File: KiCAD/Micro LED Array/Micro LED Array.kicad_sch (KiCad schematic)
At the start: 15 parts, among them J1 Conn_02x07_1mm

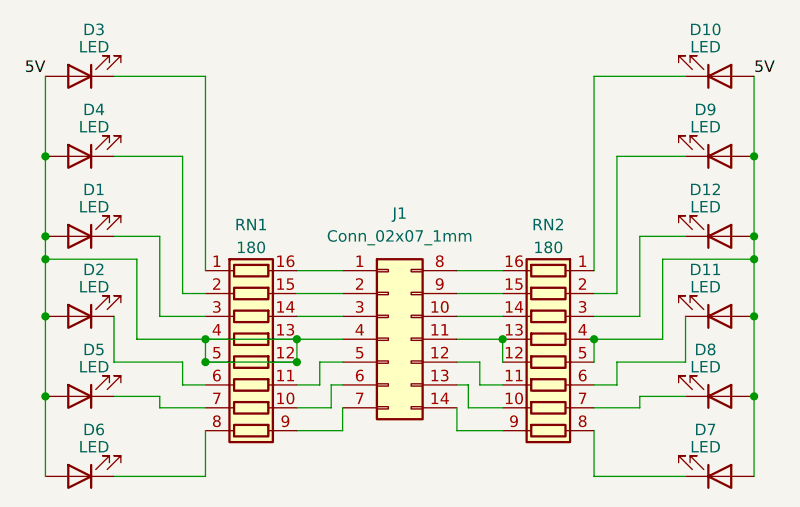
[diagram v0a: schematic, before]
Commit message: Add holes for electrodes
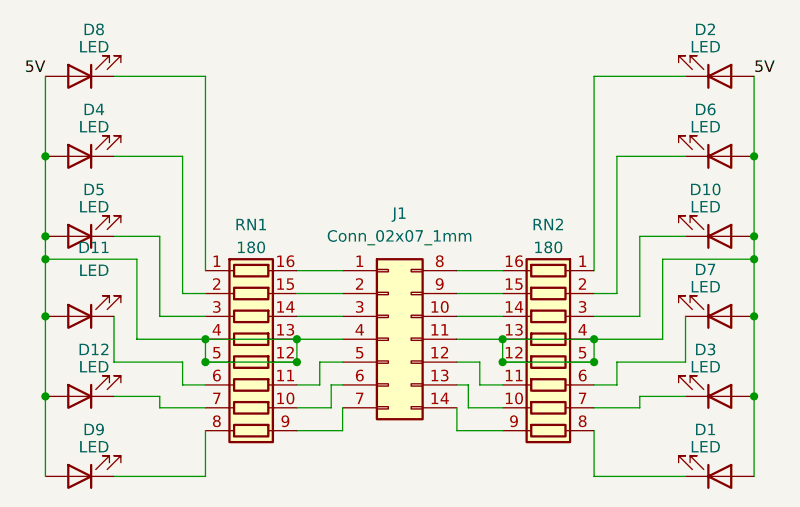
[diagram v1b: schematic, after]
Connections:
- net 5V: now also J1.11 (Pin_11), RN2.12 (R5.2), RN2.13 (R4.2)
- net at RN1.1 (R1.1): now also D8.1 (K); no longer D3.1 (K)
- net at RN1.3 (R3.1): now also D5.1 (K); no longer D1.1 (K)
- net at RN1.6 (R6.1): now also D11.1 (K); no longer D2.1 (K)
- net at RN1.7 (R7.1): now also D12.1 (K); no longer D5.1 (K)
- net at RN1.8 (R8.1): now also D9.1 (K); no longer D6.1 (K)
- net at RN2.2 (R2.1): now also D6.1 (K); no longer D9.1 (K)
- net at RN2.3 (R3.1): now also D10.1 (K); no longer D12.1 (K)
- net at RN2.1 (R1.1): now also D2.1 (K); no longer D10.1 (K)
- net at D7.1 (K): now also RN2.6 (R6.1); no longer RN2.8 (R8.1)
- net at RN2.7 (R7.1): now also D3.1 (K); no longer D8.1 (K)
- new net: D1.1 (K), RN2.8 (R8.1)
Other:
- moved on the sheet: D1, D10, D11, D12, D2, D3, D5, D6, D7, D8, D9
